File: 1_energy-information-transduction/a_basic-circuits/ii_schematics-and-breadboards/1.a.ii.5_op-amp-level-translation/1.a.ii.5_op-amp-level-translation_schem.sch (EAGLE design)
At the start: 16 parts, among them IC1 TL072P, Q1 IRF540, Q2 IRF540

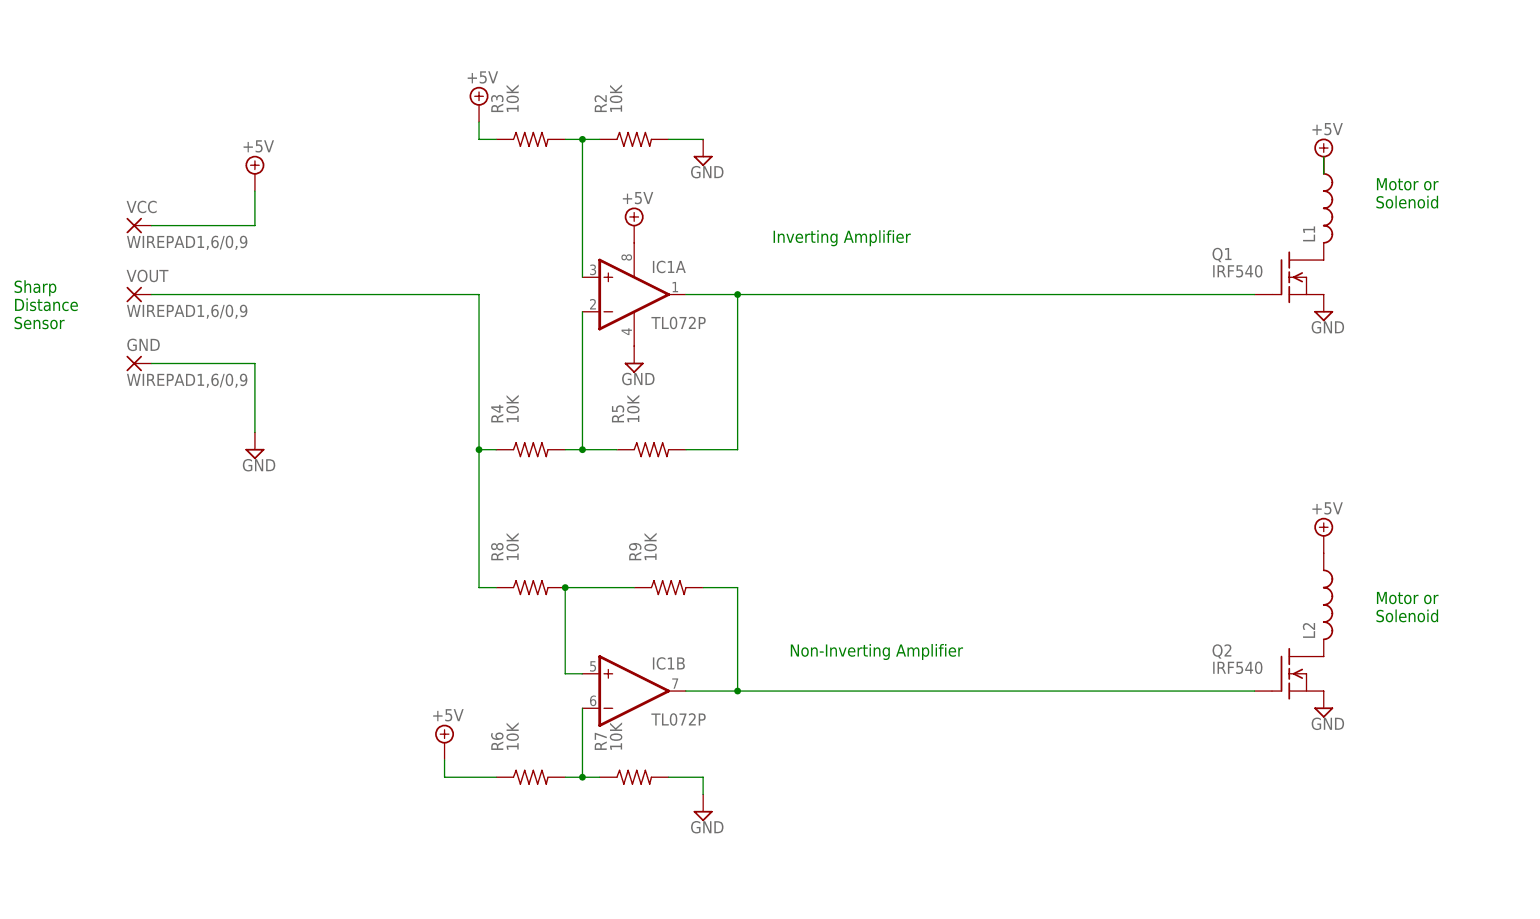
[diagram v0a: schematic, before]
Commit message: Finishing first version of op-amp exercise.
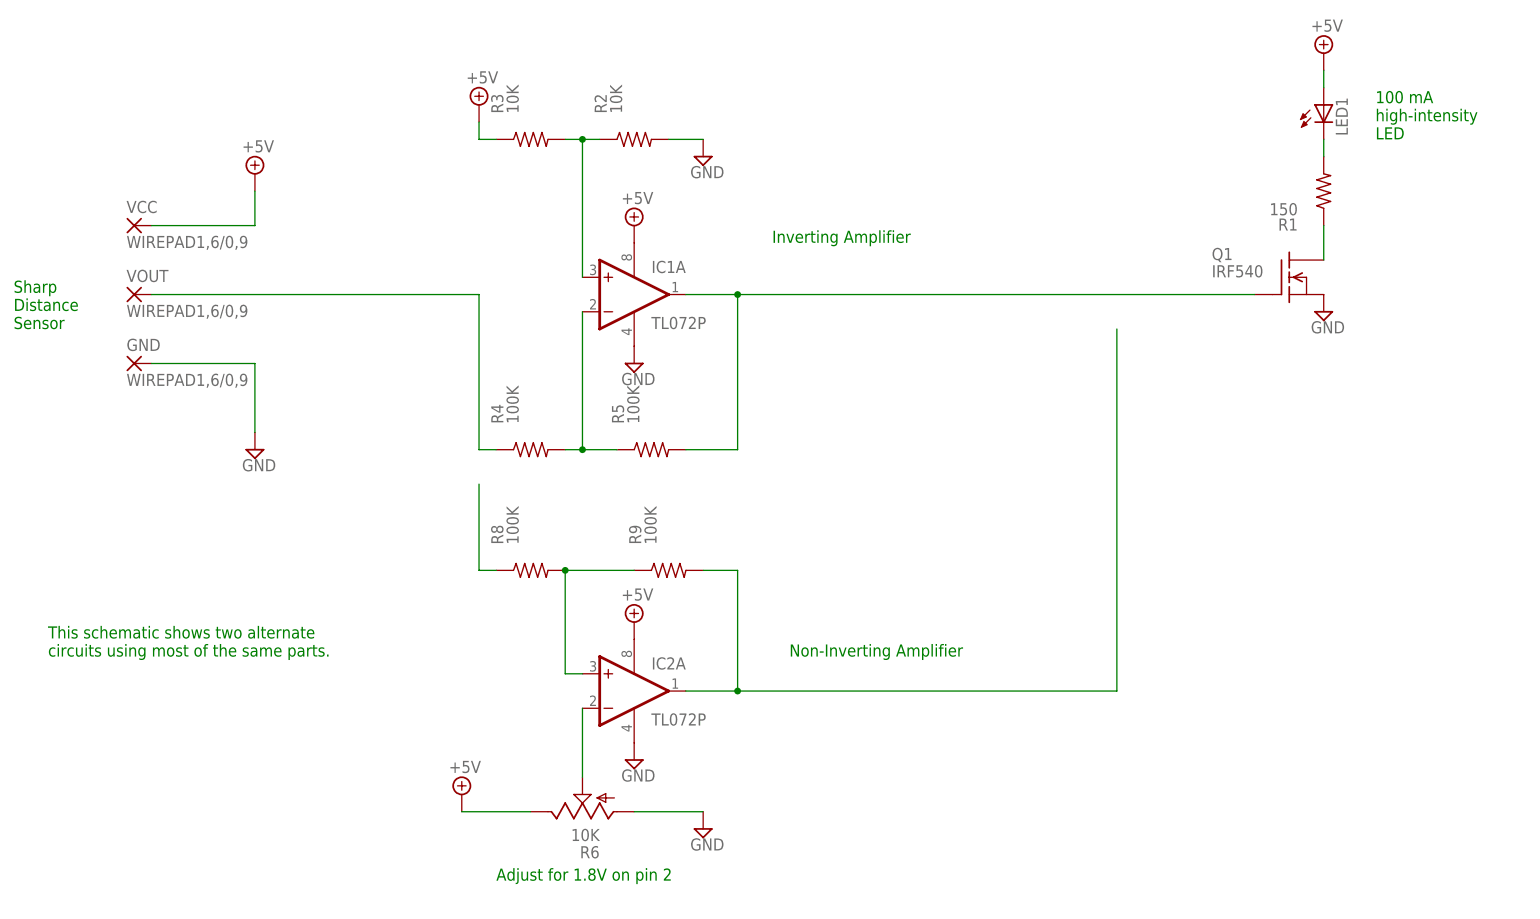
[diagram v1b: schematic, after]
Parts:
- removed L1, L2: (no value), rcl:L-US0207/7
- removed Q2: IRF540, transistor-fet:IRF540
- removed R7: 10K, resistor:R-US_0204/7
- added IC2: TL072P, linear:TL072P
- added LED1: (no value), led:LED10MM
- added R1: 150, resistor:R-US_0204/7
- R4, R5, R8, R9: value 10K -> 100K
- R6: device resistor:R-US_0204/7 -> pot:TRIM_US-B25V
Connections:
- new net N$10: R8.1
- net +5V: now also IC2P.V+, LED1.A; no longer L1.1, L2.1, R6.1
- net GND: now also IC2P.V-; no longer Q2.S, R7.2
- net N$2: now also LED1.C, R1.2; no longer L2.2, Q2.D
- net N$3: no longer R8.1
- net N$6: now also IC2A.+IN; no longer IC1B.+IN
- net N$7: now also IC2A.OUT; no longer IC1B.OUT
- net N$8: now also IC2A.-IN, R6.S; no longer IC1B.-IN, R6.2, R7.1
- net N$9: now also R1.1; no longer L1.2
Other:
- note added: "100 mA high-intensity LED"
- note added: "Adjust for 1.8V on pin 2"
- note added: "This schematic shows two alternate circuits using most of the same parts."
- note removed: "Motor or Solenoid"
- moved on the sheet: R8, R9

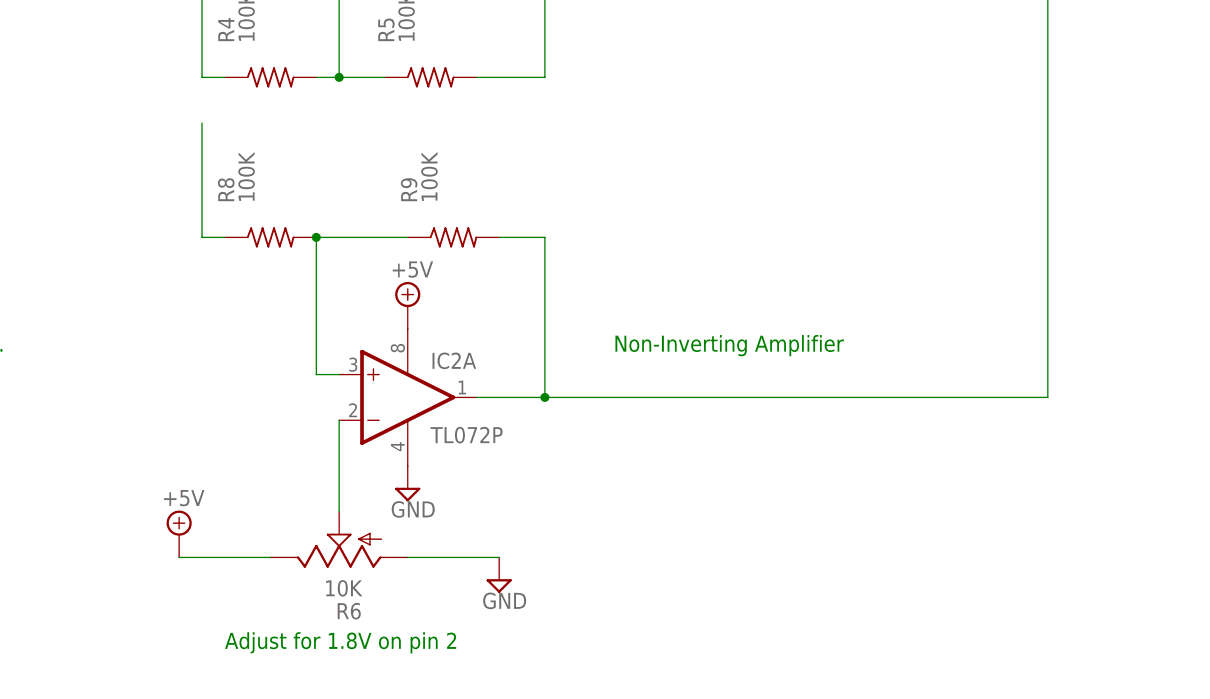
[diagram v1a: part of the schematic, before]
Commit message: Fixing error in non-inverting op-amp circuit.
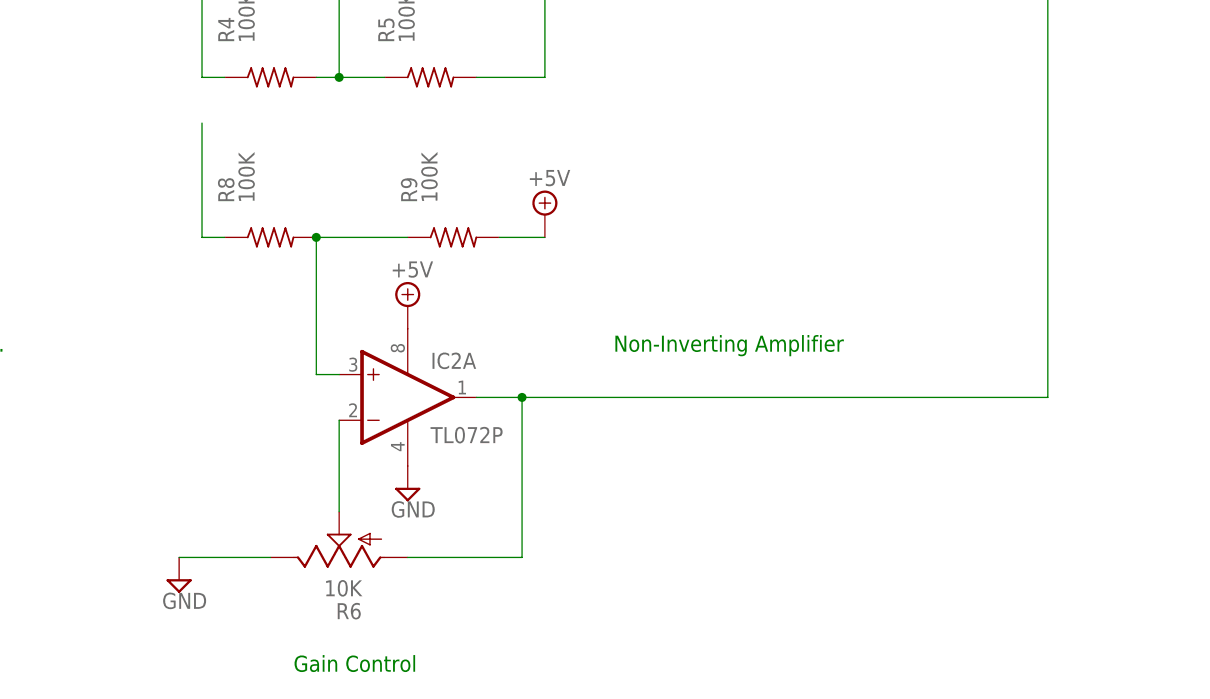
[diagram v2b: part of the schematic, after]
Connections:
- removed net N$7: IC2A.OUT, R9.2
- new net N$11: IC2A.OUT
- net +5V: now also R9.2
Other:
- note added: "Gain Control"
- note removed: "Adjust for 1.8V on pin 2"
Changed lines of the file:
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@@
 <part name="SUPPLY7" library="supply2" deviceset="+5V" device=""/>
 <part name="SUPPLY8" library="supply2" deviceset="GND" device=""/>
-<part name="SUPPLY9" library="supply2" deviceset="GND" device=""/>
-<part name="SUPPLY10" library="supply2" deviceset="+5V" device=""/>
 <part name="R8" library="resistor" deviceset="R-US_" device="0204/7" value="100K"/>
 <part name="R9" library="resistor" deviceset="R-US_" device="0204/7" value="100K"/>
@@
 <part name="SUPPLY13" library="supply2" deviceset="GND" device=""/>
 <part name="SUPPLY14" library="supply2" deviceset="+5V" device=""/>
+<part name="SUPPLY1" library="supply2" deviceset="GND" device=""/>
+<part name="SUPPLY9" library="supply2" deviceset="+5V" device=""/>
 </parts>
 <sheets>
@@
 high-intensity
 LED</text>
-<text x="88.9" y="33.02" size="1.778" layer="91">Adjust for 1.8V on pin 2</text>
 <text x="22.86" y="66.04" size="1.778" layer="91">This schematic shows two alternate
 circuits using most of the same parts.</text>
+<text x="96.52" y="30.48" size="1.778" layer="91">Gain Control</text>
 </plain>
 <instances>
@@
 <instance part="SUPPLY7" gate="+5V" x="86.36" y="147.32"/>
 <instance part="SUPPLY8" gate="GND" x="119.38" y="139.7"/>
-<instance part="SUPPLY9" gate="GND" x="119.38" y="40.64"/>
-<instance part="SUPPLY10" gate="+5V" x="83.82" y="45.72"/>
 <instance part="R8" gate="G$1" x="93.98" y="78.74" smashed="yes">
 <attribute name="NAME" x="89.9414" y="82.55" size="1.778" layer="95" rot="R90"/>
@@
 <instance part="SUPPLY14" gate="+5V" x="109.22" y="71.12"/>
 <instance part="IC2" gate="P" x="109.22" y="60.96"/>
+<instance part="SUPPLY1" gate="GND" x="83.82" y="40.64"/>
+<instance part="SUPPLY9" gate="+5V" x="124.46" y="81.28"/>
 </instances>
 <busses>
@@
 </segment>
 <segment>
-<pinref part="SUPPLY9" gate="GND" pin="GND"/>
-<wire x1="109.22" y1="43.18" x2="119.38" y2="43.18" width="0.1524" layer="91"/>
-</segment>
-<segment>
 <pinref part="Q1" gate="G$1" pin="S"/>
 <pinref part="SUPPLY2" gate="GND" pin="GND"/>
@@
 <pinref part="SUPPLY13" gate="GND" pin="GND"/>
 <pinref part="IC2" gate="P" pin="V-"/>
+</segment>
+<segment>
+<wire x1="93.98" y1="43.18" x2="83.82" y2="43.18" width="0.1524" layer="91"/>
+<pinref part="SUPPLY1" gate="GND" pin="GND"/>
 </segment>
 </net>
@@
 </segment>
 <segment>
-<pinref part="SUPPLY10" gate="+5V" pin="+5V"/>
-<wire x1="93.98" y1="43.18" x2="83.82" y2="43.18" width="0.1524" layer="91"/>
-</segment>
-<segment>
 <pinref part="LED1" gate="G$1" pin="A"/>
 <pinref part="SUPPLY11" gate="+5V" pin="+5V"/>
@@
 <pinref part="SUPPLY14" gate="+5V" pin="+5V"/>
 <pinref part="IC2" gate="P" pin="V+"/>
+</segment>
+<segment>
+<pinref part="R9" gate="G$1" pin="2"/>
+<wire x1="119.38" y1="78.74" x2="124.46" y2="78.74" width="0.1524" layer="91"/>
+<pinref part="SUPPLY9" gate="+5V" pin="+5V"/>
 </segment>
 </net>
@@
 </segment>
 </net>
-<net name="N$7" class="0">
-<segment>
-<pinref part="R9" gate="G$1" pin="2"/>
-<wire x1="119.38" y1="78.74" x2="124.46" y2="78.74" width="0.1524" layer="91"/>
-<wire x1="124.46" y1="78.74" x2="124.46" y2="60.96" width="0.1524" layer="91"/>
-<wire x1="124.46" y1="60.96" x2="116.84" y2="60.96" width="0.1524" layer="91"/>
-<pinref part="IC2" gate="A" pin="OUT"/>
-<wire x1="124.46" y1="60.96" x2="180.34" y2="60.96" width="0.1524" layer="91"/>
-<wire x1="180.34" y1="60.96" x2="180.34" y2="114.3" width="0.1524" layer="91"/>
-<junction x="124.46" y="60.96"/>
-</segment>
-</net>
 <net name="N$8" class="0">
 <segment>
@@
 </segment>
 </net>
+<net name="N$11" class="0">
+<segment>
+<wire x1="109.22" y1="43.18" x2="121.92" y2="43.18" width="0.1524" layer="91"/>
+<pinref part="IC2" gate="A" pin="OUT"/>
+<wire x1="116.84" y1="60.96" x2="121.92" y2="60.96" width="0.1524" layer="91"/>
+<wire x1="121.92" y1="60.96" x2="180.34" y2="60.96" width="0.1524" layer="91"/>
+<wire x1="180.34" y1="60.96" x2="180.34" y2="114.3" width="0.1524" layer="91"/>
+<wire x1="121.92" y1="43.18" x2="121.92" y2="60.96" width="0.1524" layer="91"/>
+<junction x="121.92" y="60.96"/>
+</segment>
+</net>
